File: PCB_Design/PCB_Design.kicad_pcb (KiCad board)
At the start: 2 copper layers, 54 parts, among them IC1 MIC37303YME, J1 TP4056, J2 632723300011, SW1 SW_Push, SW2 SW_Push, U1 ESP32-WROOM-32

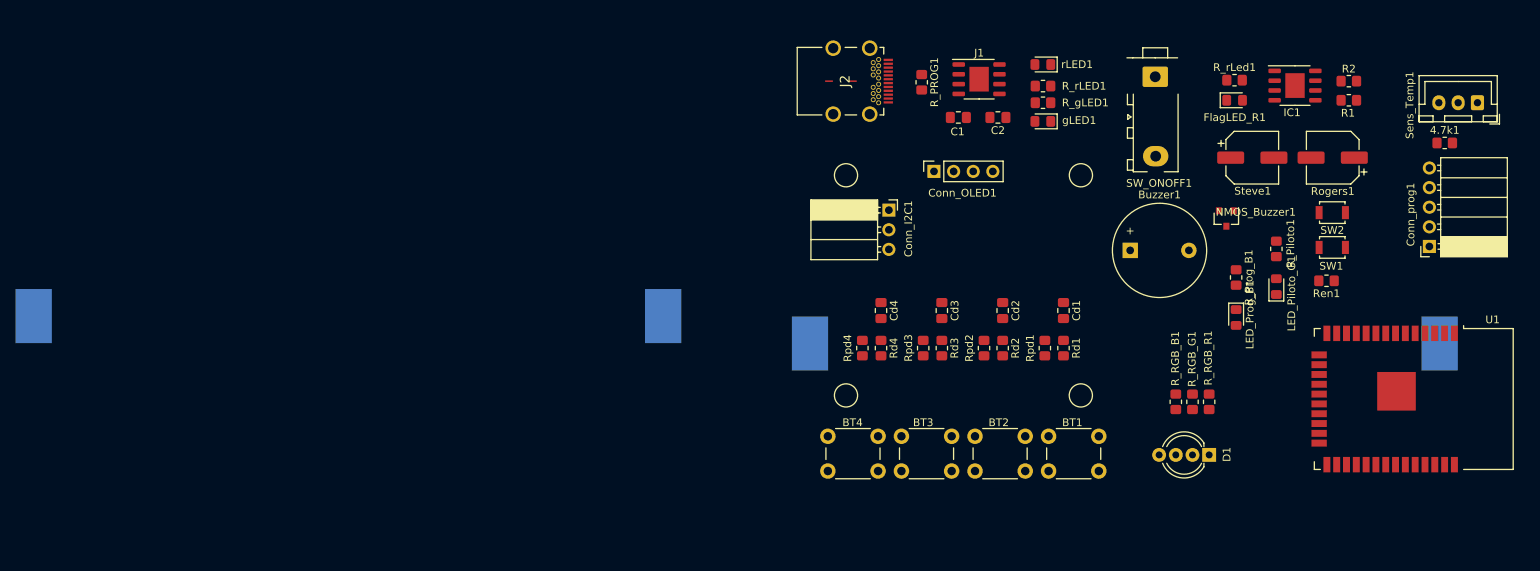
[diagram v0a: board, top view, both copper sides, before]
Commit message: PCB organizada con casi todo SMD
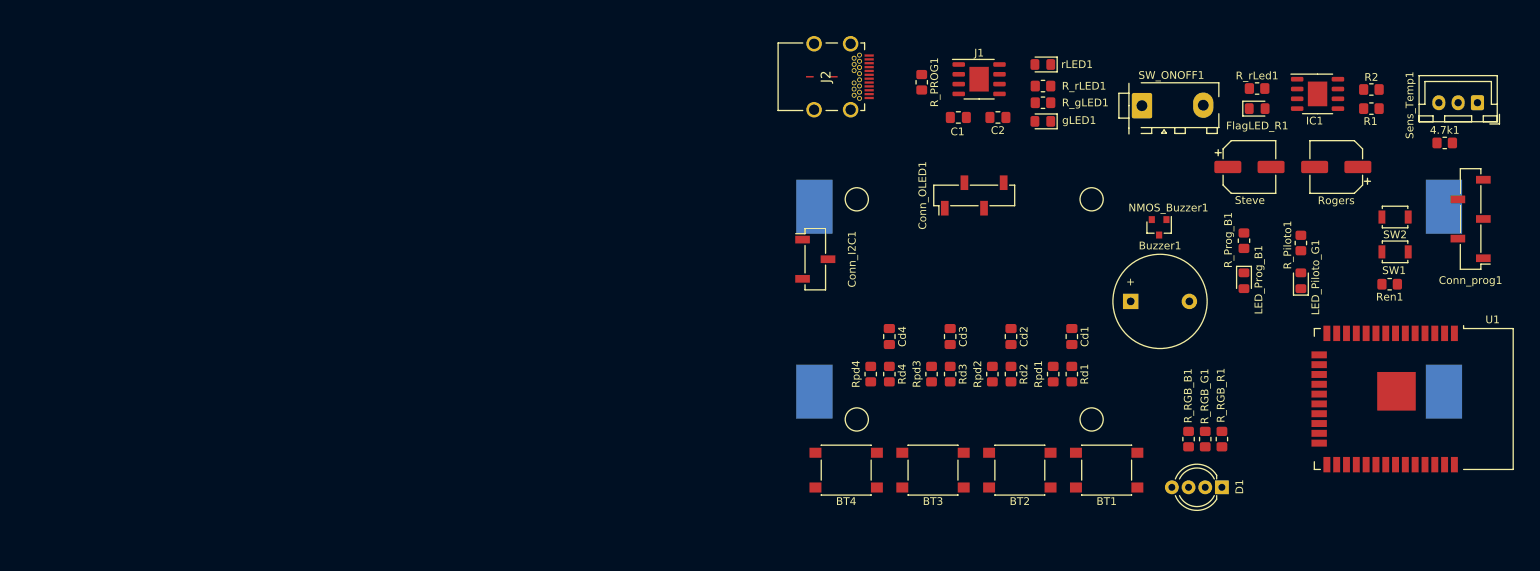
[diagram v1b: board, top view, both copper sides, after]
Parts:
- removed Rogers1, Steve1: 47u, Capacitor_SMD:CP_Elec_6.3x5.9
- added Rogers: 47u, Capacitor_SMD:CP_Elec_6.3x5.9, F.Cu at (134.6, 109.9)
- added Steve: 47u, Capacitor_SMD:CP_Elec_6.3x5.9, F.Cu at (123.4, 109.9)
- BT1, BT2, BT3, BT4: footprint Button_Switch_THT:SW_PUSH_6mm_H9.5mm -> Button_Switch_SMD:SW_Push_1P1T_NO_6x6mm_H9.5mm
- Conn_I2C1: footprint Connector_PinSocket_2.54mm:PinSocket_1x03_P2.54mm_Horizontal -> Connector_PinSocket_2.54mm:PinSocket_1x03_P2.54mm_Vertical_SMD_Pin1Left
- Conn_OLED1: footprint Connector_PinSocket_2.54mm:PinSocket_1x04_P2.54mm_Vertical -> Connector_PinSocket_2.54mm:PinSocket_1x04_P2.54mm_Vertical_SMD_Pin1Left
- Conn_prog1: footprint Connector_PinSocket_2.54mm:PinSocket_1x05_P2.54mm_Horizontal -> Connector_PinSocket_2.54mm:PinSocket_1x05_P2.54mm_Vertical_SMD_Pin1Left
- moved Battery2 32.3 mm to (71.8, 115.1), turned to 0 degrees
- moved Conn_I2C1 11.4 mm to (67.2, 121.9)
- moved NMOS_Buzzer1 8.77 mm to (111.7, 117.7)
- moved Ren1 8.19 mm to (141.5, 125.1)
- moved SW1 8.15 mm to (142.2, 120.9)
- moved SW2 8.15 mm to (142.2, 116.4)
- moved Buzzer1 6.60 mm to (108.0, 127.3)
- moved Conn_prog1 6.41 mm to (152.0, 116.6)
- moved Battery1 6.25 mm to (71.8, 139.0)
- moved Conn_OLED1 6.07 mm to (87.8, 113.6)
- moved R_RGB_B1 5.10 mm to (115.5, 145.1)
- moved R_RGB_G1 5.10 mm to (117.7, 145.1)
- moved R_RGB_R1 5.10 mm to (119.8, 145.1)
- moved LED_Prog_B1 4.87 mm to (122.7, 124.6)
- moved R_Prog_B1 4.87 mm to (122.7, 119.5)
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
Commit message: un poco mas de aire
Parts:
- moved Cd2 2.68 mm to (92.8, 129.2)
- moved Cd3 2.68 mm to (84.9, 129.2)
- moved Rd2 2.68 mm to (92.8, 134.1)
- moved Rd3 2.68 mm to (84.9, 134.1)
- moved Rpd2 2.68 mm to (90.4, 134.1)
- moved Rpd3 2.68 mm to (82.5, 134.1)
- moved Cd1 2.68 mm to (100.6, 129.2)
- moved Cd4 2.68 mm to (77.0, 129.2)
- moved Rd1 2.68 mm to (100.6, 134.1)
- moved Rd4 2.68 mm to (77.0, 134.1)
- moved Rpd1 2.68 mm to (98.2, 134.1)
- moved Rpd4 2.68 mm to (74.6, 134.1)
- moved SW_ONOFF1 2.45 mm to (113.0, 99.6)
- moved Buzzer1 1.85 mm to (109.9, 127.2)
- moved Conn_OLED1 1.84 mm to (87.7, 111.8)
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
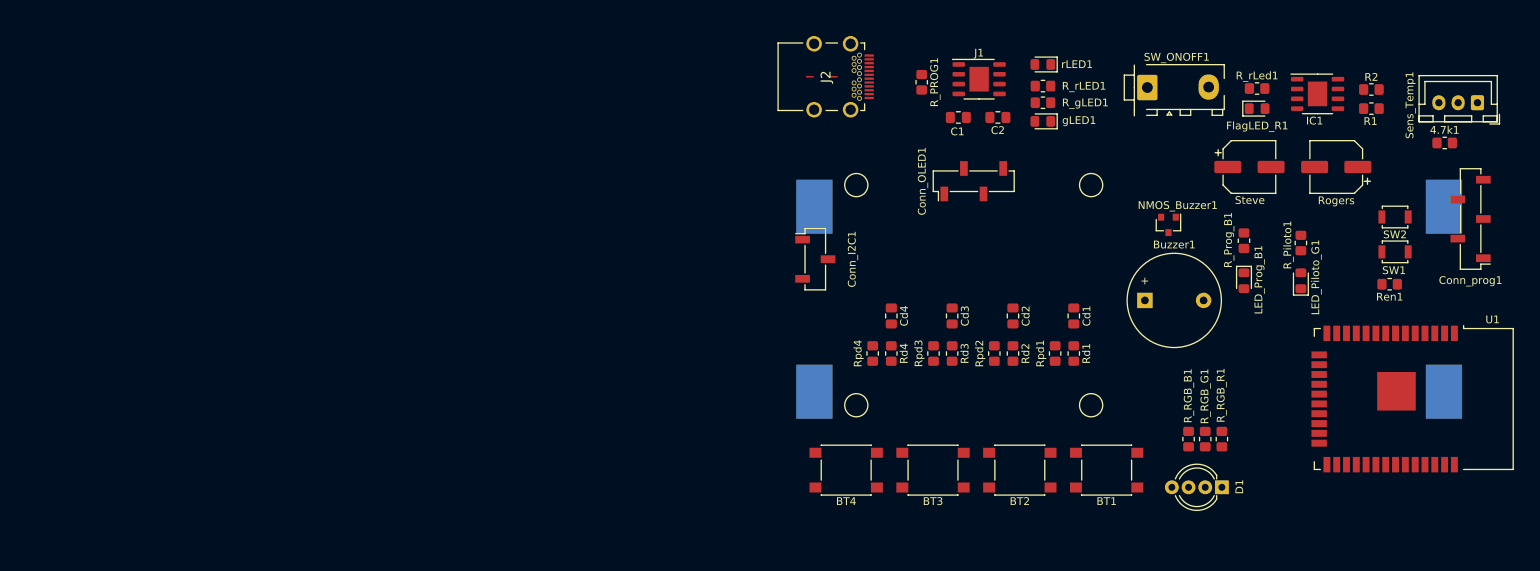
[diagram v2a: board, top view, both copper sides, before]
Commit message: Caminos de la PCB sin GND
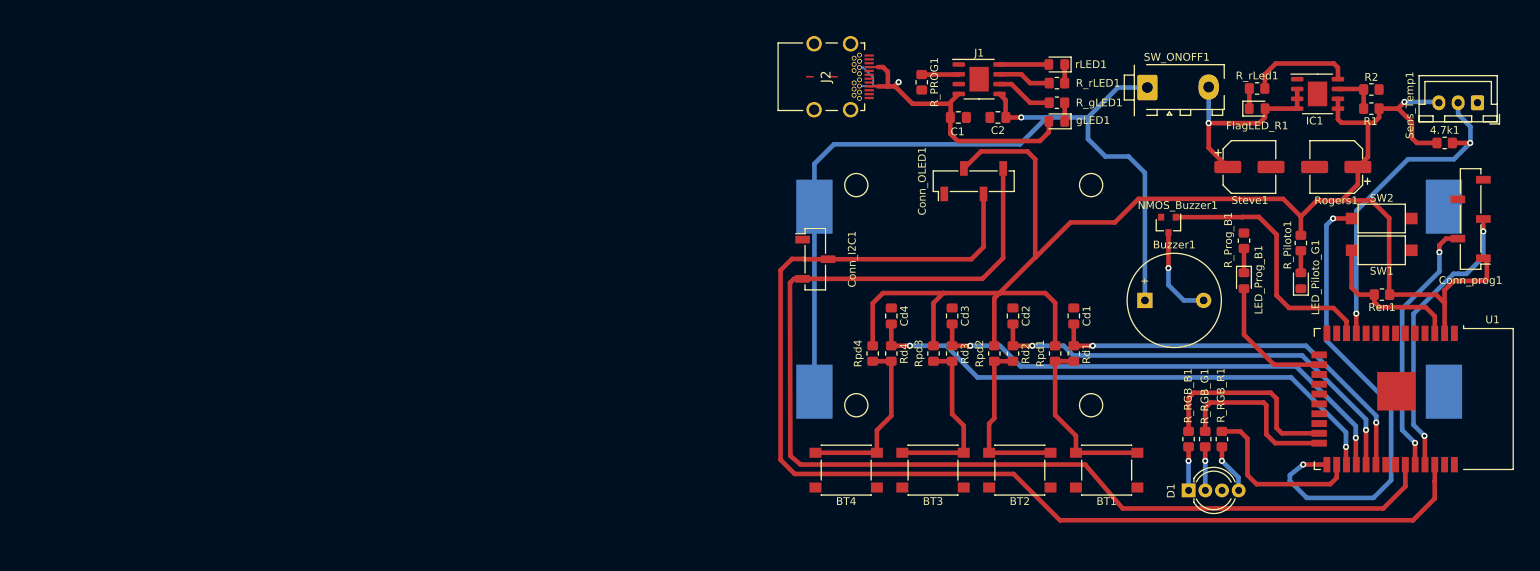
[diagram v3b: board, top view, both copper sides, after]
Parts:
- SW1, SW2: footprint Button_Switch_SMD:SW_SPST_B3U-1000P -> Button_Switch_SMD:SW_SPST_CK_RS282G05A3
- moved D1 4.32 mm to (115.5, 151.8), turned to 0 degrees
- moved R_rLED1 1.84 mm to (98.5, 99.1)
- moved R_gLED1 1.80 mm to (98.5, 101.6)
- moved gLED1 1.80 mm to (98.4, 104.0)
- moved rLED1 1.80 mm to (98.4, 96.6)
- moved SW1 1.74 mm to (140.5, 120.7)
- moved SW2 1.74 mm to (140.5, 116.6)
- moved Ren1 1.67 mm to (140.5, 126.4)
- renumbered Rogers to Rogers1, Steve to Steve1
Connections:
- Conn_OLED1 pad 3: Net-(Conn_I2C1-Pad3) -> Net-(Conn_I2C1-Pad2)
- Conn_OLED1 pad 4: Net-(Conn_I2C1-Pad2) -> Net-(Conn_I2C1-Pad3)
- D1 pad 3: Net-(D1-Pad3) -> GND
- D1 pad 4: GND -> Net-(D1-Pad4)
- R_RGB_B1 pad 1: Net-(D1-Pad3) -> Net-(D1-Pad1)
- R_RGB_R1 pad 1: Net-(D1-Pad1) -> Net-(D1-Pad4)
- U1 pad 10: Net-(R_RGB_G1-Pad2) -> Net-(U1-Pad10)
- U1 pad 11: Net-(R_RGB_R1-Pad2) -> Net-(4.7k1-Pad2)
- U1 pad 23: Net-(U1-Pad23) -> Net-(R_RGB_B1-Pad2)
- U1 pad 24: Net-(U1-Pad24) -> Net-(R_RGB_G1-Pad2)
- U1 pad 26: Net-(U1-Pad26) -> Net-(R_RGB_R1-Pad2)
- U1 pad 27: Net-(4.7k1-Pad2) -> /Button4/Sw
- U1 pad 28: Net-(U1-Pad28) -> /Button3/Sw
- U1 pad 29: Net-(U1-Pad29) -> /Button2 /Sw
- U1 pad 30: Net-(U1-Pad30) -> /Button1/Sw
- U1 pad 33: Net-(Conn_I2C1-Pad2) -> Net-(Conn_I2C1-Pad3)
- U1 pad 36: Net-(Conn_I2C1-Pad3) -> Net-(Conn_I2C1-Pad2)
- U1 pad 37: Net-(R_RGB_B1-Pad2) -> Net-(U1-Pad37)
- U1 pad 6: /Button2 /Sw -> Net-(U1-Pad6)
- U1 pad 7: /Button1/Sw -> Net-(U1-Pad7)
- U1 pad 8: /Button4/Sw -> Net-(U1-Pad8)
- U1 pad 9: /Button3/Sw -> Net-(U1-Pad9)
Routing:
- net /3.3v: track 0.00 -> 203.6 mm, vias 0 -> 1
- net Net-(Conn_I2C1-Pad2): track 0.00 -> 152.5 mm
- net Net-(Conn_I2C1-Pad3): track 0.00 -> 149.5 mm
- net /Batt: track 0.00 -> 113.9 mm, vias 0 -> 1
- net /Button4/Sw: track 0.00 -> 70.6 mm, vias 0 -> 2
- net /Button3/Sw: track 0.00 -> 64.4 mm, vias 0 -> 2
- net Net-(SW2-Pad1): track 0.00 -> 61.1 mm, vias 0 -> 2
- net /Button2 /Sw: track 0.00 -> 58.3 mm, vias 0 -> 2
- net /Button1/Sw: track 0.00 -> 52.1 mm, vias 0 -> 2
- net Net-(C1-Pad1): track 0.00 -> 46.3 mm, vias 0 -> 1
- net Net-(4.7k1-Pad2): track 0.00 -> 42.4 mm, vias 0 -> 2
- net Net-(Conn_prog1-Pad3): track 0.00 -> 37.2 mm, vias 0 -> 2
- net Net-(NMOS_Buzzer1-Pad1): track 0.00 -> 33.9 mm
- net Net-(Conn_prog1-Pad2): track 0.00 -> 33.9 mm, vias 0 -> 2
- net Net-(FlagLED_R1-Pad2): track 0.00 -> 26.8 mm, vias 0 -> 1
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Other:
- rule trace_min: 0.2 -> 0.25

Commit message: PCB finalizada
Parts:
- moved J2 1.46 mm to (66.8, 98.2)
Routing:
- net GND: track 0.00 -> 11.9 mm, vias 0 -> 7
- net Net-(C1-Pad1): track 46.3 -> 53.5 mm
- added copper zone on B.Cu, net GND
- added copper zone on F.Cu, net GND
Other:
- board outline added: 97.6 x 66.4 mm

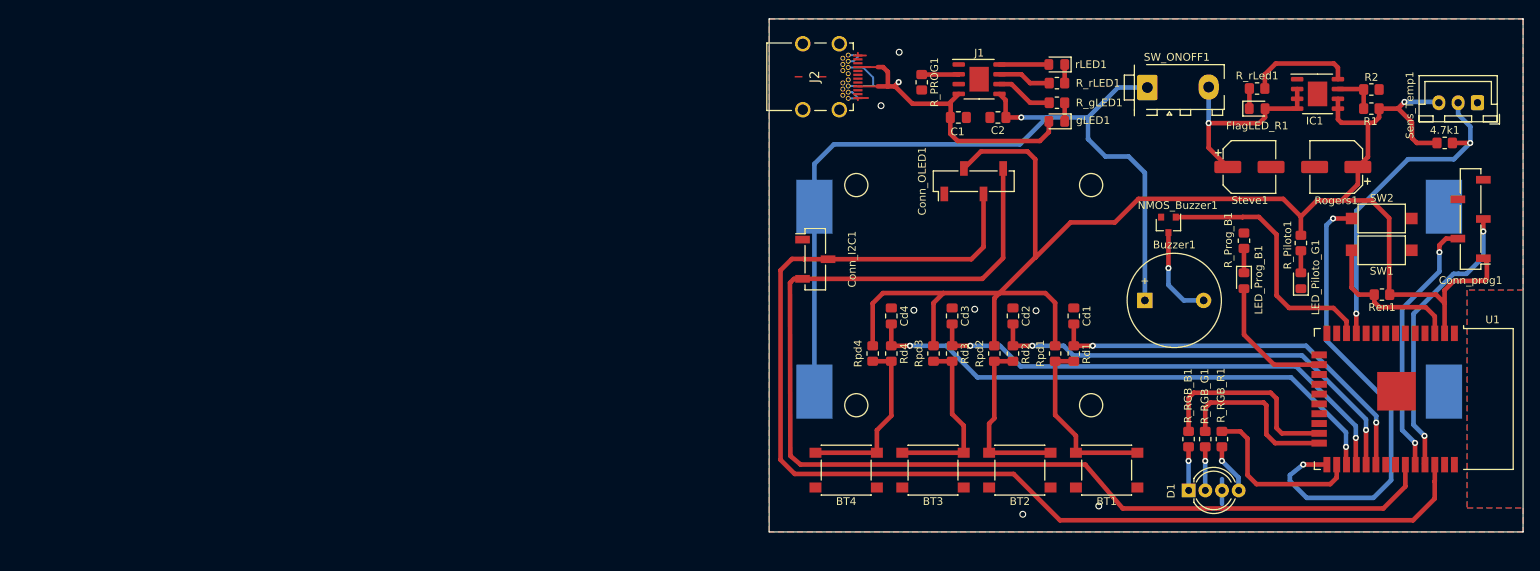
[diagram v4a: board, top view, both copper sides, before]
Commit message: Screws added succesfully
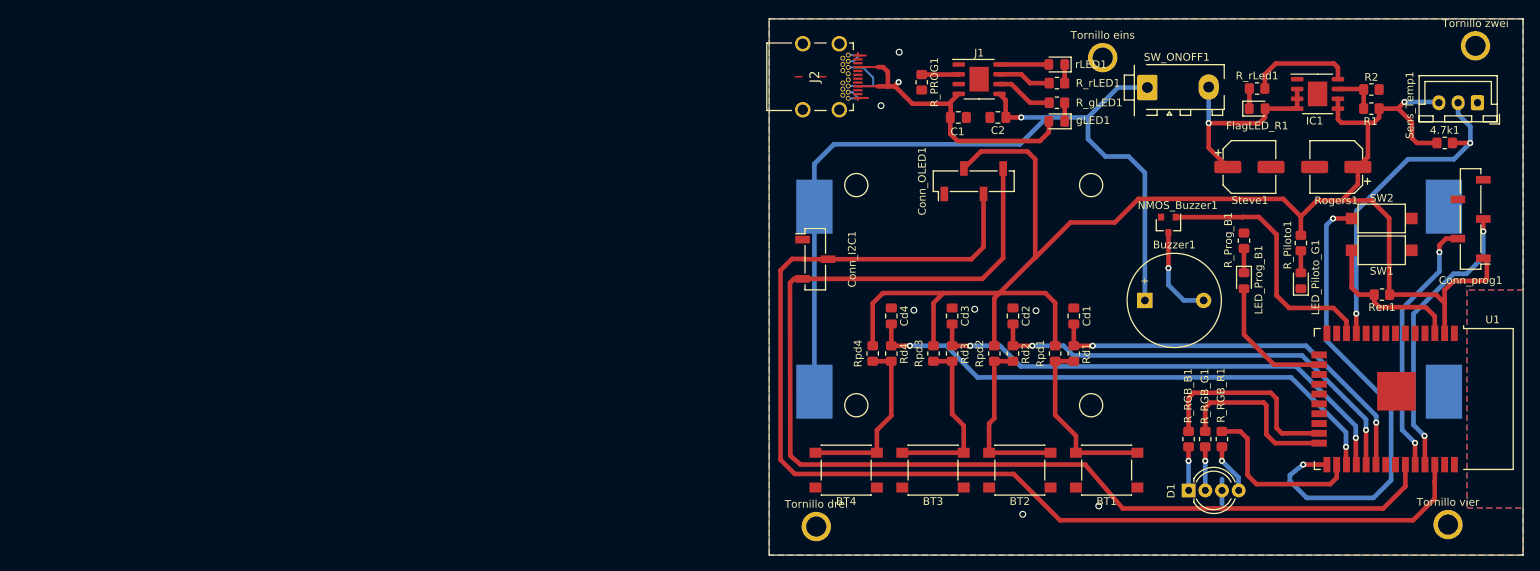
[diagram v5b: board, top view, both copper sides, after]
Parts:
- added Tornillo drei: MountingHole_2.2mm_M2_DIN965_Pad, MountingHole:MountingHole_2.2mm_M2_DIN965_Pad, F.Cu at (67.3, 156.5)
- added Tornillo eins: MountingHole_2.2mm_M2_DIN965_Pad, MountingHole:MountingHole_2.2mm_M2_DIN965_Pad, F.Cu at (104.4, 95.8)
- added Tornillo vier: MountingHole_2.2mm_M2_DIN965_Pad, MountingHole:MountingHole_2.2mm_M2_DIN965_Pad, F.Cu at (149.1, 156.2)
- added Tornillo zwei: MountingHole_2.2mm_M2_DIN965_Pad, MountingHole:MountingHole_2.2mm_M2_DIN965_Pad, F.Cu at (152.7, 94.2)
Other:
- board size 97.6 x 66.4 mm -> 97.6 x 69.4 mm

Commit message: Creación archivos gerber
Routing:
- net GND: vias 7 -> 11
